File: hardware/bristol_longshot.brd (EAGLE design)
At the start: 12 x 50 mm, 42 parts, among them U1 SAM_D20E, U2 SI4060, U4 ADP1607ACPZN-R7, U5 S25FS-S

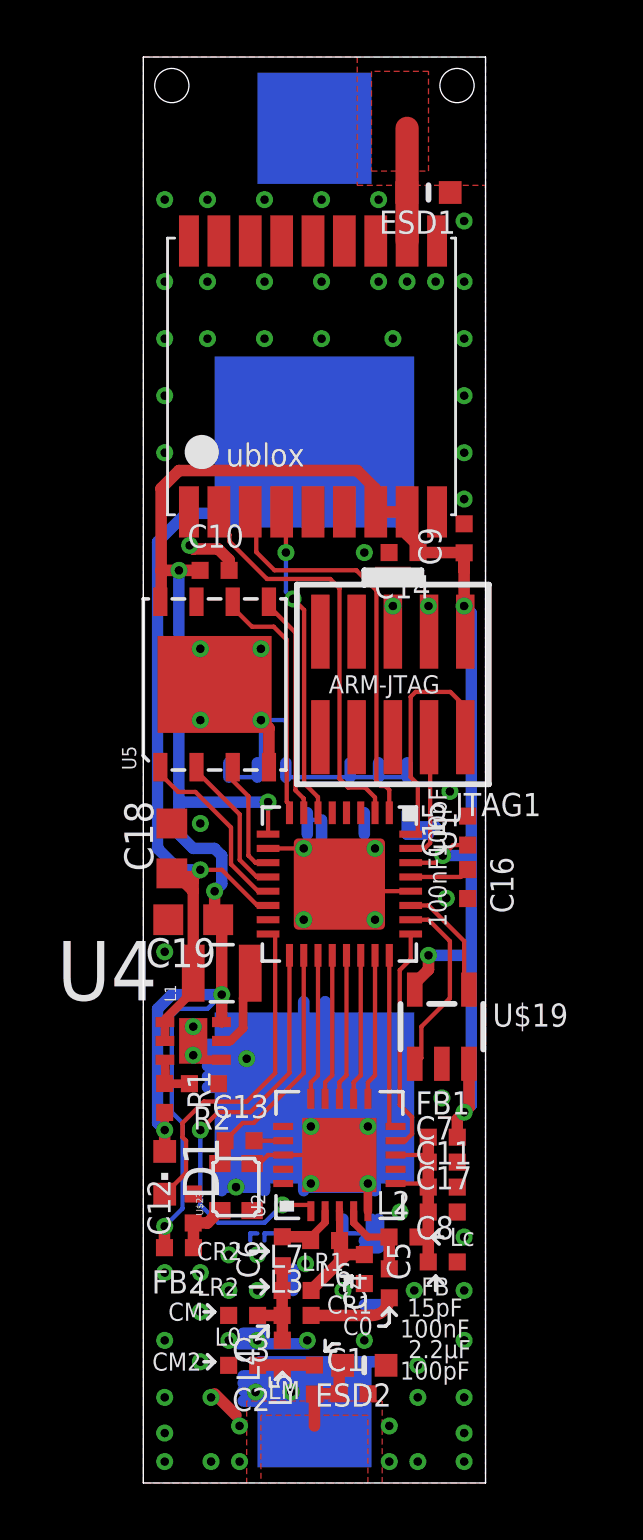
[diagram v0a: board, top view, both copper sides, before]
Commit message: Added !MR link to cortex debug connex, allows programming but not debugging of boards with watchdog enabled
Boards with watchdogs mounted can be programmed by holding !MR low. On blackmagic `mon conn e`
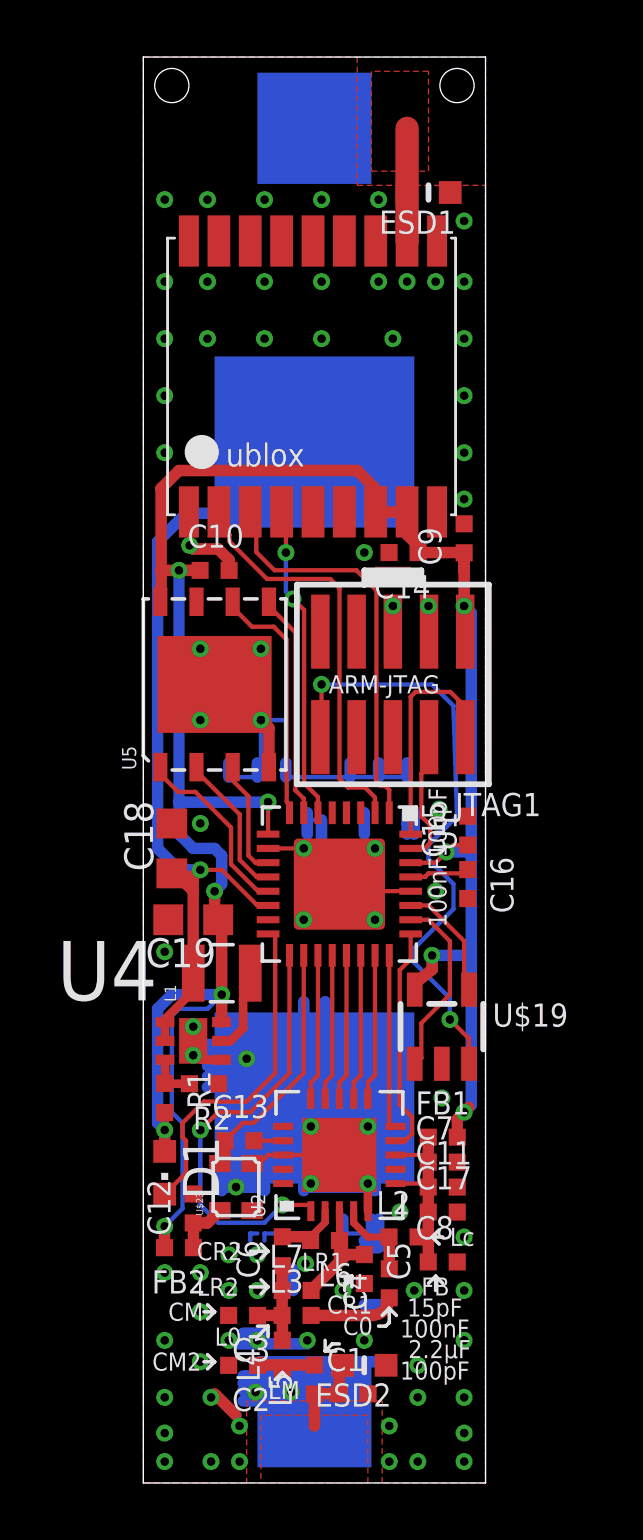
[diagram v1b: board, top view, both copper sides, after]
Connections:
- new net !MR: JTAG1.10, U$19.3
- net 1.8V: no longer U$19.3
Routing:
- net !MR: track 0.00 -> 21.5 mm, vias 0 -> 2
- net 1.8V: track 89.3 -> 87.6 mm
- net GND: track 76.1 -> 74.6 mm
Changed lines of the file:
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@@
 <?xml version="1.0" encoding="utf-8"?>
 <!DOCTYPE eagle SYSTEM "eagle.dtd">
-<eagle version="6.6.0">
+<eagle version="6.5.0">
 <drawing>
 <settings>
@@
 <contactref element="C17" pad="2"/>
 <contactref element="C11" pad="2"/>
-<via x="10.75" y="24.25" extent="1-16" drill="0.3"/>
+<via x="10.375" y="23.625" extent="1-16" drill="0.3"/>
 <via x="4.125" y="26.75" extent="1-16" drill="0.3"/>
 <via x="4.125" y="29.25" extent="1-16" drill="0.3"/>
@@
 <wire x1="5.75" y1="23.5" x2="5.75" y2="22.75" width="0.4064" layer="16"/>
 <wire x1="6.25" y1="23.25" x2="6.25" y2="22.5" width="0.4064" layer="16"/>
-<wire x1="9.25" y1="23.5" x2="9.25" y2="22.75" width="0.4064" layer="16"/>
+<wire x1="9.25" y1="23.5" x2="9.25" y2="23.125" width="0.4064" layer="16"/>
 <wire x1="9.5" y1="23.5" x2="9.5" y2="23" width="0.4064" layer="16"/>
 <wire x1="9.5" y1="23" x2="9.5" y2="22.75" width="0.4064" layer="16"/>
-<wire x1="9.25" y1="22.75" x2="10" y2="22.75" width="0.4064" layer="16"/>
-<wire x1="9.5" y1="23" x2="10.25" y2="23" width="0.4064" layer="16"/>
+<wire x1="9.25" y1="22.75" x2="9.25" y2="23.125" width="0.4064" layer="16"/>
 <wire x1="7.75" y1="23.5" x2="7.75" y2="22.75" width="0.4064" layer="16"/>
 <wire x1="5.75" y1="23.5" x2="5.75" y2="23.25" width="0.1524" layer="16"/>
@@
 <contactref element="C12" pad="2"/>
 <via x="7.75" y="32.625" extent="1-16" drill="0.3"/>
-<via x="10.625" y="20.5" extent="1-16" drill="0.3"/>
+<via x="10.25" y="20.75" extent="1-16" drill="0.3"/>
 <contactref element="R2" pad="1"/>
 <contactref element="C18" pad="2"/>
@@
 <wire x1="10.7656" y1="27.7384" x2="11.29" y2="27.214" width="0.1524" layer="1"/>
 <wire x1="11.29" y1="27.214" x2="11.29" y2="26.15" width="0.1524" layer="1"/>
-<wire x1="9.375" y1="22.75" x2="9.625" y2="22.75" width="0.1524" layer="1"/>
-<wire x1="9.625" y1="22.75" x2="9.625" y2="24.5" width="0.1524" layer="1"/>
-<wire x1="9.625" y1="24.5" x2="9.375" y2="24.75" width="0.1524" layer="1"/>
-<wire x1="9.375" y1="24.75" x2="9.375" y2="27.567" width="0.1524" layer="1"/>
+<wire x1="9.375" y1="22.75" x2="9.375" y2="27.567" width="0.1524" layer="1"/>
 </signal>
 <signal name="SWDCLK">
@@
 <wire x1="9.868" y1="22.25" x2="10.0584" y2="22.4404" width="0.1524" layer="1"/>
 <wire x1="10.0798" y1="25.0714" x2="10.02" y2="25.1312" width="0.1524" layer="1"/>
-<wire x1="10.0584" y1="22.4404" x2="10.0584" y2="25.5866" width="0.1524" layer="1"/>
+<wire x1="10.0584" y1="22.4404" x2="10.0584" y2="23.0666" width="0.1524" layer="1"/>
+<wire x1="10.0584" y1="23.0666" x2="9.75" y2="23.375" width="0.1524" layer="1"/>
+<wire x1="9.75" y1="23.375" x2="9.75" y2="24.875" width="0.1524" layer="1"/>
+<wire x1="9.75" y1="24.875" x2="10" y2="25.125" width="0.1524" layer="1"/>
 <wire x1="10.0584" y1="25.5866" x2="10.02" y2="25.625" width="0.1524" layer="1"/>
+<wire x1="10" y1="25.125" x2="10.0138" y2="25.125" width="0.1524" layer="1"/>
+<wire x1="10.0138" y1="25.125" x2="10.02" y2="25.1312" width="0.1524" layer="1"/>
 </signal>
 <signal name="KEY">
@@
 <wire x1="4.375" y1="23.875" x2="4.375" y2="22.75" width="0.1524" layer="1"/>
 <contactref element="U$19" pad="5"/>
-<contactref element="U$19" pad="3"/>
-<via x="10" y="18.5" extent="1-16" drill="0.3"/>
+<via x="10.125" y="18.5" extent="1-16" drill="0.3"/>
 <wire x1="9.51875" y1="17.3001" x2="9.5" y2="17.3501" width="0.4064" layer="1"/>
 <wire x1="9.5" y1="17.3501" x2="9.5" y2="17.5" width="0.4064" layer="1"/>
-<wire x1="9.5" y1="17.5" x2="10" y2="18" width="0.4064" layer="1"/>
-<wire x1="10" y1="18" x2="10" y2="18.5" width="0.4064" layer="1"/>
-<via x="10.5" y="22" extent="1-16" drill="0.3"/>
+<wire x1="9.5" y1="17.5" x2="10.125" y2="18" width="0.4064" layer="1"/>
+<wire x1="10.125" y1="18" x2="10.125" y2="18.5" width="0.4064" layer="1"/>
+<via x="10.625" y="22.125" extent="1-16" drill="0.3"/>
 <wire x1="9.375" y1="21.75" x2="10.25" y2="21.75" width="0.1524" layer="1"/>
-<wire x1="10.25" y1="21.75" x2="10.5" y2="22" width="0.1524" layer="1"/>
+<wire x1="10.25" y1="21.75" x2="10.625" y2="22.125" width="0.1524" layer="1"/>
 <wire x1="11.375" y1="22.367" x2="10.867" y2="22.367" width="0.1524" layer="1"/>
-<wire x1="10.867" y1="22.367" x2="10.5" y2="22" width="0.1524" layer="1"/>
+<wire x1="10.867" y1="22.367" x2="10.625" y2="22.125" width="0.1524" layer="1"/>
 <wire x1="11.25" y1="30.75" x2="11.5" y2="30.5" width="0.4" layer="16"/>
 <wire x1="11.29" y1="29.85" x2="11.25" y2="29.89" width="0.4064" layer="1"/>
 <wire x1="11.25" y1="29.89" x2="11.25" y2="30.75" width="0.4064" layer="1"/>
-<wire x1="11.5" y1="30.5" x2="11.5" y2="22" width="0.4" layer="16"/>
-<wire x1="11.5" y1="22" x2="11.5" y2="18.5" width="0.4" layer="16"/>
+<wire x1="11.5" y1="30.5" x2="11.5" y2="22.125" width="0.4" layer="16"/>
+<wire x1="11.5" y1="22.125" x2="11.5" y2="18.5" width="0.4" layer="16"/>
 <wire x1="11.5" y1="18.5" x2="11.5" y2="13.25" width="0.4" layer="16"/>
 <wire x1="11.5" y1="13.25" x2="11.25" y2="13" width="0.4" layer="16"/>
-<wire x1="10.5" y1="22" x2="11.5" y2="22" width="0.4" layer="16"/>
+<wire x1="10.625" y1="22.125" x2="11.5" y2="22.125" width="0.4" layer="16"/>
 <wire x1="11.008" y1="12.125" x2="11.008" y2="12.758" width="0.4" layer="1"/>
 <wire x1="11.008" y1="12.758" x2="11.25" y2="13" width="0.4" layer="1"/>
@@
 <wire x1="1.25" y1="16.625" x2="2.25" y2="16.625" width="0.1524" layer="16"/>
 <wire x1="2.25" y1="16.625" x2="2.75" y2="17.125" width="0.1524" layer="16"/>
-<wire x1="10" y1="18.5" x2="11.5" y2="18.5" width="0.4" layer="16"/>
-<wire x1="11.41875" y1="14.6999" x2="11.41875" y2="13.16875" width="0.4064" layer="1"/>
+<wire x1="10.125" y1="18.5" x2="11.5" y2="18.5" width="0.4" layer="16"/>
 <wire x1="11.41875" y1="13.16875" x2="11.25" y2="13" width="0.4064" layer="1"/>
 <via x="1.25" y="32" extent="1-16" drill="0.3"/>
@@
 <contactref element="U1" pad="29"/>
 <contactref element="C16" pad="1"/>
-<wire x1="9.375" y1="21.25" x2="11.133" y2="21.25" width="0.1524" layer="1"/>
-<wire x1="11.133" y1="21.25" x2="11.133" y2="21.266" width="0.1524" layer="1"/>
-<wire x1="11.133" y1="21.266" x2="11.375" y2="21.508" width="0.1524" layer="1"/>
+<wire x1="9.375" y1="21.25" x2="9.883" y2="21.25" width="0.1524" layer="1"/>
+<wire x1="9.883" y1="21.25" x2="9.883" y2="21.258" width="0.1524" layer="1"/>
+<wire x1="9.883" y1="21.258" x2="10" y2="21.375" width="0.1524" layer="1"/>
+<wire x1="10" y1="21.375" x2="11.242" y2="21.375" width="0.1524" layer="1"/>
+<wire x1="11.242" y1="21.375" x2="11.375" y2="21.508" width="0.1524" layer="1"/>
 </signal>
 <signal name="SI_SCLK">
@@
 </signal>
 <signal name="!RESET">
-<contactref element="U1" pad="26"/>
 <contactref element="U$19" pad="1"/>
-<wire x1="9.375" y1="19.75" x2="10" y2="19.75" width="0.1524" layer="1"/>
 <wire x1="10" y1="19.75" x2="10.75" y2="19" width="0.1524" layer="1"/>
-<wire x1="10.75" y1="19" x2="10.75" y2="17" width="0.1524" layer="1"/>
-<wire x1="10.75" y1="17" x2="9.75" y2="16" width="0.1524" layer="1"/>
-<wire x1="9.75" y1="16" x2="9.75" y2="14.8999" width="0.1524" layer="1"/>
+<wire x1="10.75" y1="19" x2="10.75" y2="17.125" width="0.1524" layer="1"/>
+<wire x1="10.75" y1="17.125" x2="9.75" y2="16.125" width="0.1524" layer="1"/>
+<wire x1="9.75" y1="16.125" x2="9.75" y2="14.8999" width="0.1524" layer="1"/>
 <wire x1="9.75" y1="14.8999" x2="9.51875" y2="14.6999" width="0.1524" layer="1"/>
+<contactref element="U1" pad="26"/>
+<wire x1="10" y1="19.75" x2="9.375" y2="19.75" width="0.1524" layer="1"/>
 </signal>
 <signal name="WDI">
@@
 <contactref element="U$2" pad="+1"/>
 </signal>
+<signal name="!MR">
+<contactref element="U$19" pad="3"/>
+<contactref element="JTAG1" pad="10"/>
+<via x="6.25" y="28" extent="1-16" drill="0.3"/>
+<via x="10.75" y="16.25" extent="1-16" drill="0.3"/>
+<wire x1="11.41875" y1="14.6999" x2="11.41875" y2="15.58125" width="0.1524" layer="1"/>
+<wire x1="11.41875" y1="15.58125" x2="10.75" y2="16.25" width="0.1524" layer="1"/>
+<wire x1="6.25" y1="28" x2="6.25" y2="26.19" width="0.1524" layer="1"/>
+<wire x1="6.25" y1="26.19" x2="6.21" y2="26.15" width="0.1524" layer="1"/>
+<wire x1="10.75" y1="16.25" x2="10.75" y2="17" width="0.1524" layer="16"/>
+<wire x1="10.75" y1="17" x2="9.5" y2="18.25" width="0.1524" layer="16"/>
+<wire x1="9.5" y1="18.25" x2="9.5" y2="18.75" width="0.1524" layer="16"/>
+<wire x1="9.5" y1="18.75" x2="10.875" y2="20.125" width="0.1524" layer="16"/>
+<wire x1="10.875" y1="20.125" x2="10.875" y2="21" width="0.1524" layer="16"/>
+<wire x1="10.875" y1="21" x2="10" y2="21.875" width="0.1524" layer="16"/>
+<wire x1="10" y1="21.875" x2="10" y2="22.375" width="0.1524" layer="16"/>
+<wire x1="10" y1="22.375" x2="11" y2="23.375" width="0.1524" layer="16"/>
+<wire x1="11" y1="23.375" x2="10.875" y2="27.25" width="0.1524" layer="16"/>
+<wire x1="10.875" y1="27.25" x2="10.125" y2="28" width="0.1524" layer="16"/>
+<wire x1="10.125" y1="28" x2="6.25" y2="28" width="0.1524" layer="16"/>
+</signal>
 </signals>
